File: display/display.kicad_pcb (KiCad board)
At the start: 4 copper layers, 162 x 65.4 mm, 19 parts, among them J1 DIN41612_03x32_ABC

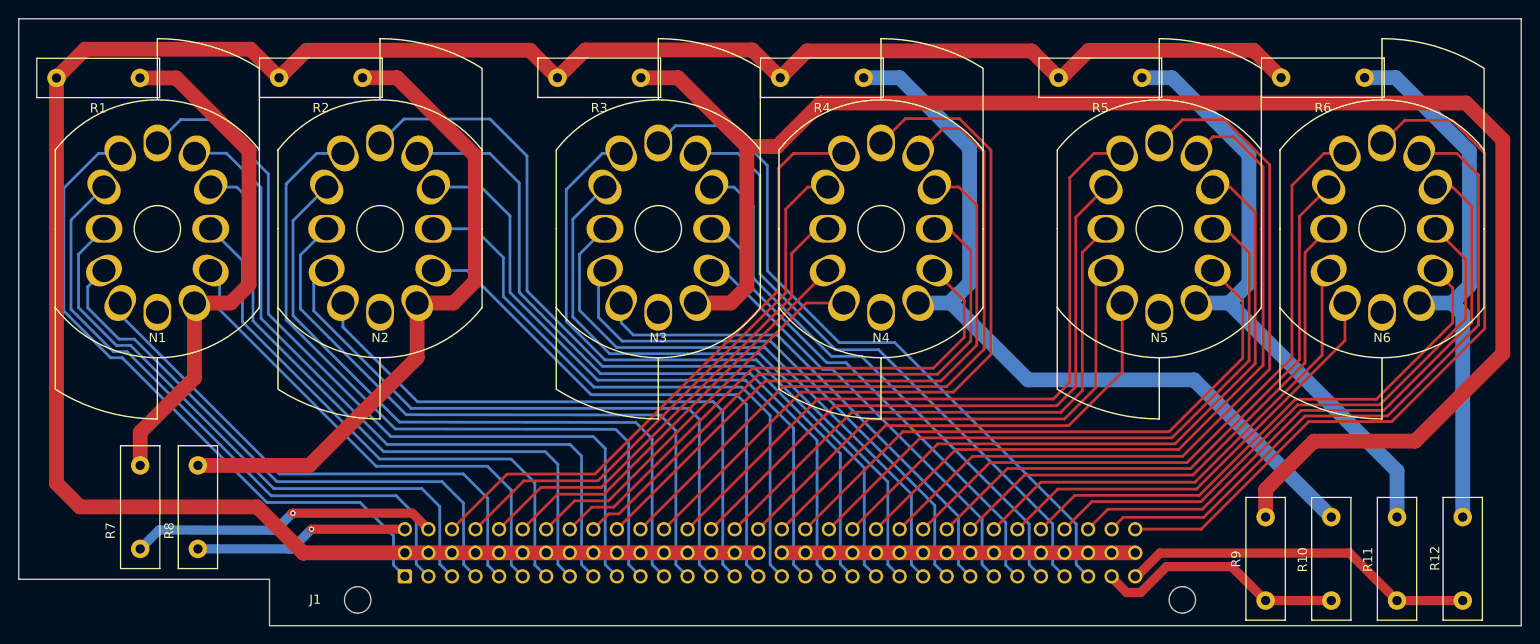
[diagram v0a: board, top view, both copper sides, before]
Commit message: Enlage notch in display board and minor fussing. New Gerbers.
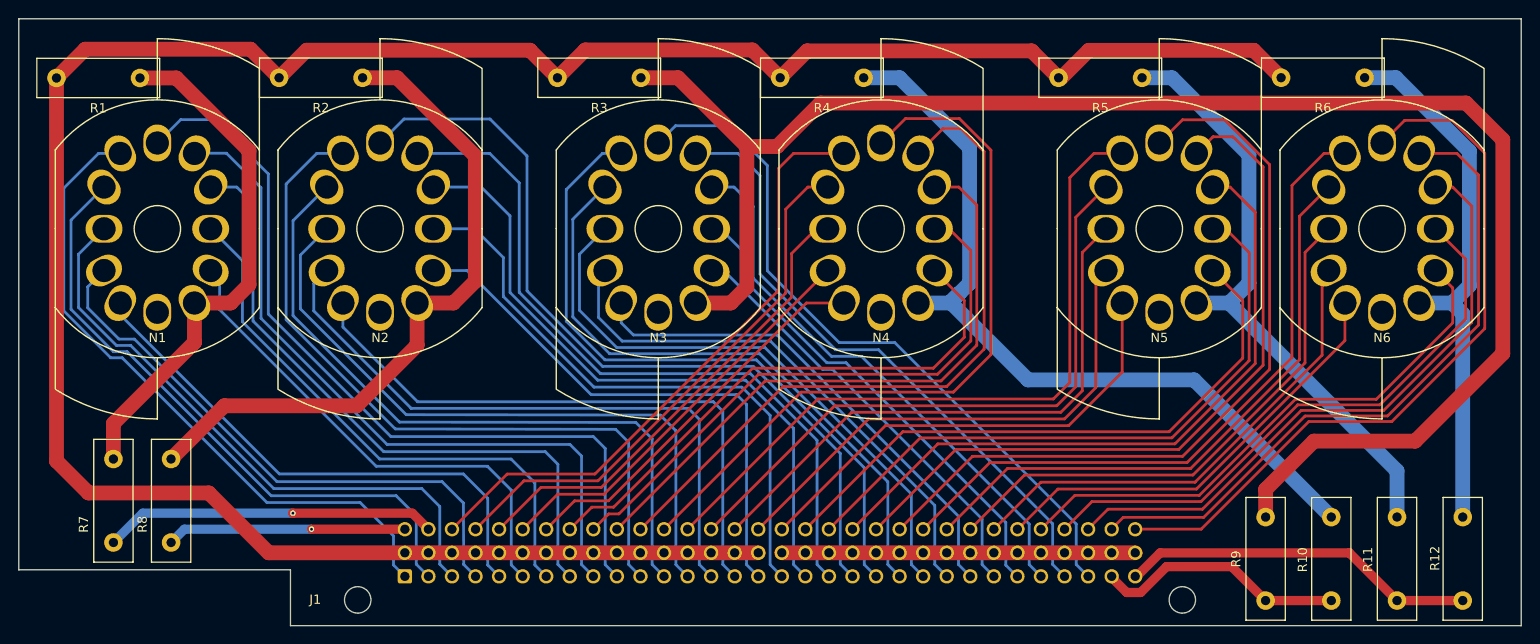
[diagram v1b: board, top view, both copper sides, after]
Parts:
- moved R7 2.97 mm to (81.6, 109.3)
- moved R8 2.97 mm to (87.8, 109.3)
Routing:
- net Net-(J1-Pin_c2): track 33.4 -> 36.0 mm
- net Net-(J1-Pin_c1): track 23.2 -> 25.8 mm
- net Net-(N2-A): track 70.7 -> 72.6 mm
- net Net-(J1-Pin_b1): track 266.9 -> 265.4 mm
- net Net-(N1-A): track 56.1 -> 56.6 mm
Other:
- outline, holes or cut-outs redrawn
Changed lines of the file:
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@@
 	)
 	(footprint "Resistor_THT:R_Box_L13.0mm_W4.0mm_P9.00mm"
-		(locked yes)
 		(layer "F.Cu")
-		(at 84.45 109.96 -90)
+		(at 81.56 109.27 -90)
 		(descr "Resistor, Box series, Radial, pin pitch=9.00mm, 2W, length*width=13.0*4.0mm^2, http://www.produktinfo.conrad.com/datenblaetter/425000-449999/443860-da-01-de-METALLBAND_WIDERSTAND_0_1_OHM_5W_5Pr.pdf")
 		(tags "Resistor Box series Radial pin pitch 9.00mm 2W length 13.0mm width 4.0mm")
@@
 	)
 	(footprint "Resistor_THT:R_Box_L13.0mm_W4.0mm_P9.00mm"
-		(locked yes)
 		(layer "F.Cu")
-		(at 90.67 109.96 -90)
+		(at 87.78 109.27 -90)
 		(descr "Resistor, Box series, Radial, pin pitch=9.00mm, 2W, length*width=13.0*4.0mm^2, http://www.produktinfo.conrad.com/datenblaetter/425000-449999/443860-da-01-de-METALLBAND_WIDERSTAND_0_1_OHM_5W_5Pr.pdf")
 		(tags "Resistor Box series Radial pin pitch 9.00mm 2W length 13.0mm width 4.0mm")
@@
 	(gr_poly
 		(pts
-			(xy 233.3354 127.2413) (xy 98.39 127.2413) (xy 98.39 122.24) (xy 71.3582 122.24) (xy 71.3582 61.8087)
+			(xy 233.3354 127.2413) (xy 100.65 127.2413) (xy 100.65 121.22) (xy 71.3582 121.22) (xy 71.3582 61.8087)
 			(xy 233.3354 61.8087)
 		)
@@
 	)
 	(segment
-		(start 77.96 114.43)
-		(end 75.424 111.894)
-		(width 1.6)
-		(layer "F.Cu")
-		(net 7)
-	)
-	(segment
-		(start 102.045 119.415)
-		(end 97.06 114.43)
+		(start 78.87 112.93)
+		(end 75.424 109.484)
 		(width 1.6)
 		(layer "F.Cu")
@@
 	)
 	(segment
-		(start 180.5569 65.27)
-		(end 183.4569 68.17)
+		(start 75.424 109.484)
+		(end 75.424 68.19)
 		(width 1.6)
 		(layer "F.Cu")
@@
 	)
 	(segment
-		(start 102.08 119.38)
-		(end 102.045 119.415)
+		(start 180.5569 65.27)
+		(end 183.4569 68.17)
 		(width 1.6)
 		(layer "F.Cu")
@@
 	(segment
 		(start 151.08 119.38)
-		(end 102.08 119.38)
+		(end 98.3 119.38)
 		(width 1.6)
 		(layer "F.Cu")
@@
 	)
 	(segment
-		(start 156.3468 65.27)
-		(end 180.5569 65.27)
-		(width 1.6)
-		(layer "F.Cu")
-		(net 7)
-	)
-	(segment
-		(start 97.06 114.43)
-		(end 77.96 114.43)
+		(start 98.3 119.38)
+		(end 91.85 112.93)
 		(width 1.6)
 		(layer "F.Cu")
@@
 	)
 	(segment
-		(start 75.424 111.894)
-		(end 75.424 68.19)
+		(start 156.3468 65.27)
+		(end 180.5569 65.27)
 		(width 1.6)
 		(layer "F.Cu")
@@
 	)
 	(segment
+		(start 91.85 112.93)
+		(end 78.87 112.93)
+		(width 1.6)
+		(layer "F.Cu")
+		(net 7)
+	)
+	(segment
 		(start 99.424 68.17)
 		(end 102.394 65.2)
@@
 	)
 	(segment
-		(start 90.67 118.96)
-		(end 100.44 118.96)
-		(width 1)
-		(layer "B.Cu")
-		(net 45)
-	)
-	(segment
-		(start 100.79 118.96)
-		(end 102.9 116.85)
+		(start 102.92 116.84)
+		(end 89.21 116.84)
 		(width 1)
 		(layer "B.Cu")
@@
 	)
 	(segment
-		(start 100.44 118.96)
-		(end 100.79 118.96)
+		(start 89.21 116.84)
+		(end 87.78 118.27)
 		(width 1)
 		(layer "B.Cu")
@@
 	)
 	(segment
-		(start 90.296452 100.543548)
+		(start 94.2 92.45)
 		(end 90.296452 92.45)
 		(width 1.6)
@@
 	)
 	(segment
-		(start 94.2 92.45)
-		(end 90.296452 92.45)
+		(start 88.34 68.19)
+		(end 96.18 76.03)
 		(width 1.6)
 		(layer "F.Cu")
@@
 	)
 	(segment
-		(start 88.34 68.19)
-		(end 96.18 76.03)
+		(start 90.296452 92.45)
+		(end 90.296452 96.703548)
 		(width 1.6)
 		(layer "F.Cu")
@@
 	)
 	(segment
-		(start 84.424 68.19)
-		(end 88.34 68.19)
+		(start 81.56 105.44)
+		(end 81.56 109.27)
 		(width 1.6)
 		(layer "F.Cu")
@@
 	)
 	(segment
-		(start 84.45 106.39)
-		(end 90.296452 100.543548)
+		(start 84.424 68.19)
+		(end 88.34 68.19)
 		(width 1.6)
 		(layer "F.Cu")
@@
 	)
 	(segment
-		(start 84.45 109.96)
-		(end 84.45 106.39)
+		(start 90.296452 96.703548)
+		(end 81.56 105.44)
 		(width 1.6)
 		(layer "F.Cu")
@@
 	)
 	(segment
-		(start 102.69 109.96)
-		(end 114.304 98.346)
+		(start 107.78 103.53)
+		(end 93.52 103.53)
+		(width 1.6)
+		(layer "F.Cu")
+		(net 66)
+	)
+	(segment
+		(start 114.304 97.006)
+		(end 107.78 103.53)
 		(width 1.6)
 		(layer "F.Cu")
@@
 	)
 	(segment
-		(start 90.67 109.96)
-		(end 102.69 109.96)
+		(start 108.424 68.17)
+		(end 112.15 68.17)
 		(width 1.6)
 		(layer "F.Cu")
@@
 	)
 	(segment
-		(start 108.424 68.17)
-		(end 112.15 68.17)
+		(start 93.52 103.53)
+		(end 87.78 109.27)
 		(width 1.6)
 		(layer "F.Cu")
@@
 	)
 	(segment
-		(start 114.304 98.346)
+		(start 118.22 92.45)
 		(end 114.304 92.45)
 		(width 1.6)
@@
 	)
 	(segment
-		(start 118.22 92.45)
-		(end 114.304 92.45)
+		(start 114.304 92.45)
+		(end 114.304 97.006)
 		(width 1.6)
 		(layer "F.Cu")
@@
 	)
 	(segment
-		(start 191.88 121.92)
-		(end 191.72 121.92)
+		(start 194.41 119.39)
+		(end 191.88 121.92)
 		(width 1)
 		(layer "F.Cu")
@@
 	)
 	(segment
-		(start 219.946666 124.53)
-		(end 214.826666 119.41)
+		(start 214.806666 119.39)
+		(end 194.41 119.39)
 		(width 1)
 		(layer "F.Cu")
@@
 	)
 	(segment
-		(start 214.826666 119.41)
-		(end 194.39 119.41)
+		(start 219.946666 124.53)
+		(end 214.806666 119.39)
 		(width 1)
 		(layer "F.Cu")
@@
 	)
 	(segment
-		(start 194.39 119.41)
-		(end 191.88 121.92)
+		(start 191.88 121.92)
+		(end 191.72 121.92)
 		(width 1)
 		(layer "F.Cu")
@@
 	)
 	(segment
-		(start 86.49 116.92)
-		(end 99.01 116.95)
+		(start 84.72 115.11)
+		(end 81.56 118.27)
 		(width 1)
 		(layer "B.Cu")
@@
 	)
 	(segment
-		(start 99.01 116.95)
-		(end 100.82 115.14)
-		(width 1)
-		(layer "B.Cu")
-		(net 75)
-	)
-	(segment
-		(start 84.45 118.96)
-		(end 86.49 116.92)
-		(width 1)
-		(layer "B.Cu")
-		(net 75)
-	)
-	(segment
-		(start 100.82 115.14)
-		(end 100.85 115.14)
+		(start 100.91 115.11)
+		(end 84.72 115.11)
 		(width 1)
 		(layer "B.Cu")
@@
 		(polygon
 			(pts
-				(xy 233.19 126.94) (xy 233.19 121.48) (xy 98.55 121.48) (xy 98.55 126.94)
+				(xy 233.19 126.94) (xy 233.19 120.55) (xy 101.17 120.51) (xy 101.17 126.9)
 			)
 		)
@@
 		(polygon
 			(pts
-				(xy 71.49 61.95) (xy 233.22 61.95) (xy 233.22 121.84) (xy 71.5 121.84) (xy 71.49 121.83)
+				(xy 71.49 61.95) (xy 233.22 61.95) (xy 233.43 120.8) (xy 71.71 120.8) (xy 71.49 121.83)
 			)
 		)
 	)
+	(group ""
+		(members "6559a51c-0ac7-4e56-931c-6e3c767d635e" "cf8fd9d8-1b2f-40b4-97d5-73e380010358")
+	)
 )
